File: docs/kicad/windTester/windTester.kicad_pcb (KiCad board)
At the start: 2 copper layers, 59.7 x 31.7 mm, 29 parts, among them J1 Conn_01x01, J10 Conn_01x01, J2 Conn_01x01, J3 Conn_01x01, J4 Conn_01x01, J5 Conn_01x01, J6 Conn_01x01, J7 Conn_01x01, J8 Conn_01x01, J9 Conn_01x01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

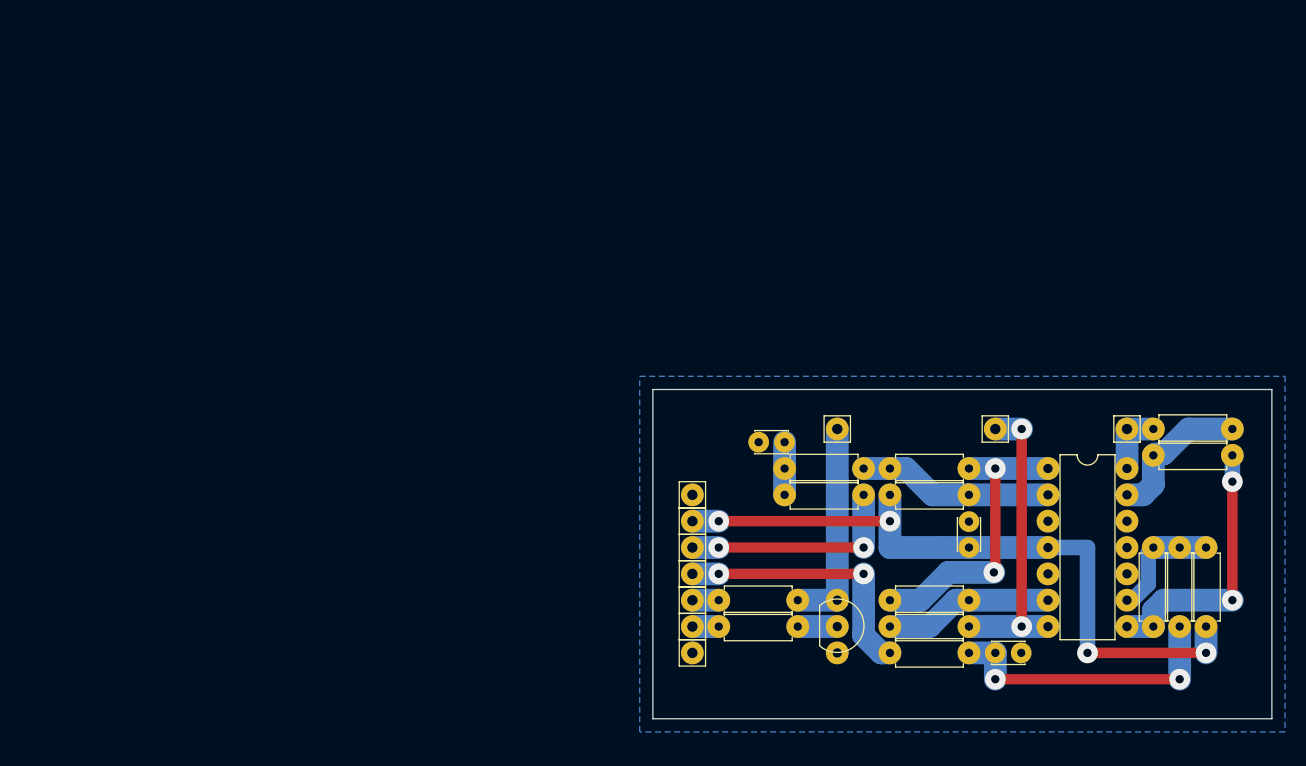
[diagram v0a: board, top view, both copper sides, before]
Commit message: Panic Checking - windTester PCB right after coPilot tells me it wont generate 2-8V preceding new design
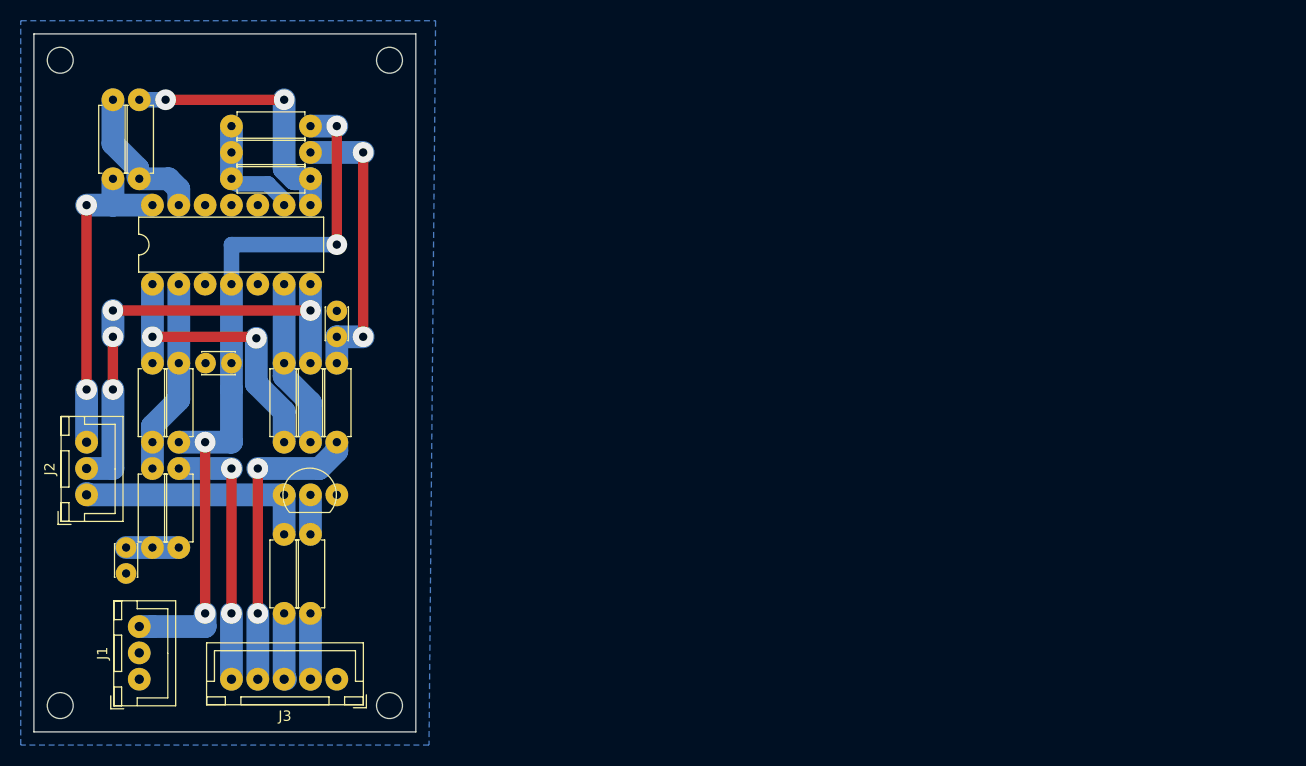
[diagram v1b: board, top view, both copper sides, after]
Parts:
- removed J10, J4, J5, J6, J7, J8, J9: Conn_01x01, 0_my_footprints:myPinHeader_1x01
- added REF**: myMountingHole_2.5mm, 0_my_footprints:myMountingHole_2.5mm, F.Cu at (27.9, 86.4)
- added REF**: myMountingHole_2.5mm, 0_my_footprints:myMountingHole_2.5mm, F.Cu at (59.7, 86.4)
- added REF**: myMountingHole_2.5mm, 0_my_footprints:myMountingHole_2.5mm, F.Cu at (59.7, 24.1)
- added REF**: myMountingHole_2.5mm, 0_my_footprints:myMountingHole_2.5mm, F.Cu at (27.9, 24.1)
- J1: value Conn_01x01 -> SEATALK; footprint 0_my_footprints:myPinHeader_1x01 -> 0_my_footprints:myJSTx03
- J2: value Conn_01x01 -> INSTRUMENT; footprint 0_my_footprints:myPinHeader_1x01 -> 0_my_footprints:myJSTx03
- J3: value Conn_01x01 -> TEENSY_PCB; footprint 0_my_footprints:myPinHeader_1x01 -> 0_my_footprints:myJSTx05
- moved R12 103.2 mm to (33.0, 35.6), turned to 90 degrees
- moved R11 101.4 mm to (35.6, 35.6), turned to 90 degrees
- moved R8 99.1 mm to (44.5, 33.0), turned to 0 degrees
- moved R9 98.9 mm to (52.1, 30.5), turned to 180 degrees
- moved R10 92.0 mm to (52.1, 35.6), turned to 180 degrees
- moved U1 88.2 mm to (36.8, 45.7), turned to 90 degrees
- moved R4 79.4 mm to (36.8, 53.3), turned to 270 degrees
- moved C3 73.3 mm to (44.5, 53.3), turned to 180 degrees
- moved C2 70.4 mm to (54.6, 50.8), turned to 90 degrees
- moved R5 69.9 mm to (49.5, 53.3), turned to 270 degrees
- moved R3 68.8 mm to (39.4, 61.0), turned to 90 degrees
- moved R2 68.6 mm to (36.8, 63.5), turned to 270 degrees
- moved R6 68.4 mm to (52.1, 53.3), turned to 270 degrees
- moved R7 67.1 mm to (54.6, 53.3), turned to 270 degrees
- moved C1 64.3 mm to (34.3, 71.1), turned to 270 degrees
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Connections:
- J1 pad 1: +12V -> GND
- J2 pad 1: GND -> WIND_SQUARE
- J3 pad 1: WIND_SQUARE -> GND
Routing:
- net SIGNALB: track 6.35 -> 31.7 mm, vias 0 -> 2
- net SIGNALA: track 29.2 -> 44.5 mm, vias 2 -> 4
- net +12V: track 67.3 -> 72.4 mm
- net +5V: track 2.54 -> 6.41 mm
- net PWMA: track 21.6 -> 25.4 mm
- net SPEED_SQUARE: track 2.54 -> 6.35 mm
- net PWMB: track 25.7 -> 29.5 mm
- net WIND_SQUARE: track 20.3 -> 22.9 mm
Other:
- board size 59.7 x 31.7 mm -> 36.8 x 67.3 mm
